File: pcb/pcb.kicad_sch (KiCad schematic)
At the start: 281 parts, among them J1 Conn_01x08_Socket, J2 Conn_01x02_Female, U1 YAAJ_WeAct_BlackPill_Part_Lik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

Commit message: attempting to add RGB
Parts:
- removed BZ1: Buzzer, symbol Device:Buzzer
- removed D18: BAV70, Keebio-Parts:SOT-23_Handsoldering, symbol Diode:BAV70
- removed MX047, MX051.125, MX062, MX063, MX066.100, MX077, MX087, MX089.100, MX099, MX109.100, MX117, MX121, MX132.225, MX136, MX137: MX-NoLED, MX_Only:MXOnly-1U-NoLED, symbol MX_Alps_Hybrid:MX-NoLED
- removed R1, R2: 470, symbol Device:R_Small
- removed R3: R_22K, Keebio-Parts:Resistor, symbol Device:R_Small
- added C1: 100n, schizobovine:C_0603_1608Metric, symbol Device:C_Small
- added FID1: Fiducial, schizobovine:COW, symbol Mechanical:Fiducial
- added LD1, LD10, LD100, LD101, LD102, LD103, LD104, LD105, LD106, LD107, LD108, LD109, LD11, LD110, LD111, LD112, LD113, LD114, LD115, LD116, LD117, LD118, LD119, LD12, LD120, LD121, LD122, LD13, LD14, LD15, LD16, LD17, LD18, LD19, LD2, LD20, LD21, LD22, LD23, LD24, LD25, LD26, LD27, LD28, LD29, LD3, LD30, LD31, LD32, LD33, LD34, LD35, LD36, LD37, LD38, LD39, LD4, LD40, LD41, LD42, LD43, LD44, LD45, LD46, LD47, LD48, LD49, LD5, LD50, LD51, LD52, LD53, LD54, LD55, LD56, LD57, LD58, LD59, LD6, LD60, LD61, LD62, LD63, LD64, LD65, LD66, LD67, LD68, LD69, LD7, LD70, LD71, LD72, LD73, LD74, LD75, LD76, LD77, LD78, LD79, LD8, LD80, LD81, LD82, LD83, LD84, LD85, LD86, LD87, LD88, LD89, LD9, LD90, LD91, LD92, LD93, LD94, LD95, LD96, LD97, LD98, LD99: WS2812B, schizobovine:LED_SK6812MINI_PLCC4_3.1x2.7mm_P1.75mm_reverse_mount, symbol LED:WS2812B
- added N1: Solenoid, schizobovine:solenoid, symbol Mechanical:Housing
- added U2: SN74LVC1G125DBV, Package_TO_SOT_SMD:SOT-23-5, symbol 74xGxx:SN74LVC1G125DBV
- H1, H10, H11, H12, H13, H14, H15, H16, H17, H18, H19, H2, H20, H21, H22, H23, H24, H25, H26, H27, H28, H29, H3, H30, H31, H32, H33, H34, H35, H36, H37, H38, H39, H4, H40, H41, H42, H43, H44, H45, H46, H47, H48, H49, H5, H50, H51, H52, H53, H54, H55, H56, H57, H58, H59, H6, H60, H61, H62, H63, H64, H65, H66, H67, H68, H69, H7, H8, H9: footprint (none) -> MountingHole:MountingHole_3mm
- J1: footprint (none) -> Connector_PinHeader_2.54mm:PinHeader_1x08_P2.54mm_Vertical
- MX000, MX001, MX002, MX003, MX004, MX005, MX006, MX007, MX009, MX012, MX013, MX014, MX015, MX016, MX017, MX018, MX019, MX020, MX021, MX022, MX023, MX024, MX025, MX026, MX027, MX028, MX029, MX030, MX032, MX033, MX034, MX035, MX036, MX037, MX038, MX039, MX040, MX042, MX043, MX044, MX045, MX046, MX048, MX049, MX050, MX052, MX053, MX054, MX055, MX056, MX057, MX058, MX059, MX060, MX065, MX067, MX068, MX069, MX072, MX073, MX074, MX075, MX076, MX078, MX079, MX082, MX083, MX084, MX085, MX086, MX088, MX090, MX091, MX092, MX093, MX094, MX095, MX096, MX097, MX098, MX100, MX101, MX102, MX103, MX104, MX105, MX106, MX107, MX108, MX110, MX111, MX112, MX113, MX114, MX115, MX116, MX117.100, MX120, MX122, MX123, MX124, MX125, MX126, MX130, MX134, MX135: footprint MX_Only:MXOnly-1U-NoLED -> MX_Only:MXOnly-1U-Hotswap
- MX008: footprint (none) -> MX_Only:MXOnly-1U-Hotswap; symbol MX_Alps_Hybrid:MX-LED -> MX_Alps_Hybrid:MX-NoLED
- MX031, MX061, MX064, MX131, MX133: footprint MX_Only:MXOnly-1U-NoLED -> MX_Only:MXOnly-1.5U-Hotswap
- MX041: value MX-LED -> MX-NoLED; footprint (none) -> MX_Only:MXOnly-1.75U-Hotswap; symbol MX_Alps_Hybrid:MX-LED -> MX_Alps_Hybrid:MX-NoLED
- MX041.125: value MX-LED -> MX-NoLED; footprint (none) -> MX_Only:MXOnly-1.25U-Hotswap; symbol MX_Alps_Hybrid:MX-LED -> MX_Alps_Hybrid:MX-NoLED
- MX047.200: footprint MX_Only:MXOnly-1U-NoLED -> MX_Only:MXOnly-ISO-Hotswap
- MX051: footprint MX_Only:MXOnly-1U-NoLED -> MX_Only:MXOnly-2.25U-Hotswap
- MX066: footprint MX_Only:MXOnly-1U-NoLED -> MX_Only:MXOnly-2U-Hotswap
- MX087.200: footprint MX_Only:MXOnly-1U-NoLED -> MX_Only:MXOnly-2U-Hotswap-ReversedStabilizers
- MX089, MX109: footprint MX_Only:MXOnly-1U-NoLED -> MX_Only:MXOnly-2U-Hotswap-ReversedVerticalStabilizers
- MX127: footprint MX_Only:MXOnly-1U-NoLED -> MX_Only:MXOnly-2.75U-Hotswap
- MX127.175: footprint MX_Only:MXOnly-1U-NoLED -> MX_Only:MXOnly-1.75U-Hotswap
- MX132: footprint MX_Only:MXOnly-1U-NoLED -> MX_Only:MXOnly-7U-Hotswap
- R4: footprint Keebio-Parts:Resistor -> Keebio-Parts:Resistor-Hybrid
- U1: footprint Kicad-STM32:YAAJ_WeAct_BlackPill_SWD_2 -> Footprints:YAAJ_WeAct_BlackPill_SWD_2
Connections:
- net +5V: now also C1.1, LD1.1 (VDD), LD10.1 (VDD), LD100.1 (VDD), LD101.1 (VDD), LD102.1 (VDD), LD103.1 (VDD), LD104.1 (VDD), LD105.1 (VDD), LD106.1 (VDD), LD107.1 (VDD), LD108.1 (VDD), LD109.1 (VDD), LD11.1 (VDD), LD110.1 (VDD), LD111.1 (VDD), LD112.1 (VDD), LD113.1 (VDD), LD114.1 (VDD), LD115.1 (VDD), LD116.1 (VDD), LD117.1 (VDD), LD118.1 (VDD), LD119.1 (VDD), LD12.1 (VDD), LD120.1 (VDD), LD121.1 (VDD), LD122.1 (VDD), LD13.1 (VDD), LD14.1 (VDD), LD15.1 (VDD), LD16.1 (VDD), LD17.1 (VDD), LD18.1 (VDD), LD19.1 (VDD), LD2.1 (VDD), LD20.1 (VDD), LD21.1 (VDD), LD22.1 (VDD), LD23.1 (VDD), LD24.1 (VDD), LD25.1 (VDD), LD26.1 (VDD), LD27.1 (VDD), LD28.1 (VDD), LD29.1 (VDD), LD3.1 (VDD), LD30.1 (VDD), LD31.1 (VDD), LD32.1 (VDD), LD33.1 (VDD), LD34.1 (VDD), LD35.1 (VDD), LD36.1 (VDD), LD37.1 (VDD), LD38.1 (VDD), LD39.1 (VDD), LD4.1 (VDD), LD40.1 (VDD), LD41.1 (VDD), LD42.1 (VDD), LD43.1 (VDD), LD44.1 (VDD), LD45.1 (VDD), LD46.1 (VDD), LD47.1 (VDD), LD48.1 (VDD), LD49.1 (VDD), LD5.1 (VDD), LD50.1 (VDD), LD51.1 (VDD), LD52.1 (VDD), LD53.1 (VDD), LD54.1 (VDD), LD55.1 (VDD), LD56.1 (VDD), LD57.1 (VDD), LD58.1 (VDD), LD59.1 (VDD), LD6.1 (VDD), LD60.1 (VDD), LD61.1 (VDD), LD62.1 (VDD), LD63.1 (VDD), LD64.1 (VDD), LD65.1 (VDD), LD66.1 (VDD), LD67.1 (VDD), LD68.1 (VDD), LD69.1 (VDD), LD7.1 (VDD), LD70.1 (VDD), LD71.1 (VDD), LD72.1 (VDD), LD73.1 (VDD), LD74.1 (VDD), LD75.1 (VDD), LD76.1 (VDD), LD77.1 (VDD), LD78.1 (VDD), LD79.1 (VDD), LD8.1 (VDD), LD80.1 (VDD), LD81.1 (VDD), LD82.1 (VDD), LD83.1 (VDD), LD84.1 (VDD), LD85.1 (VDD), LD86.1 (VDD), LD87.1 (VDD), LD88.1 (VDD), LD89.1 (VDD), LD9.1 (VDD), LD90.1 (VDD), LD91.1 (VDD), LD92.1 (VDD), LD93.1 (VDD), LD94.1 (VDD), LD95.1 (VDD), LD96.1 (VDD), LD97.1 (VDD), LD98.1 (VDD), LD99.1 (VDD), U2.5 (VCC)
- net BL_BUZ: no longer U1.7 (PA10)
- net GND: now also C1.2, LD1.3 (VSS), LD10.3 (VSS), LD100.3 (VSS), LD101.3 (VSS), LD102.3 (VSS), LD103.3 (VSS), LD104.3 (VSS), LD105.3 (VSS), LD106.3 (VSS), LD107.3 (VSS), LD108.3 (VSS), LD109.3 (VSS), LD11.3 (VSS), LD110.3 (VSS), LD111.3 (VSS), LD112.3 (VSS), LD113.3 (VSS), LD114.3 (VSS), LD115.3 (VSS), LD116.3 (VSS), LD117.3 (VSS), LD118.3 (VSS), LD119.3 (VSS), LD12.3 (VSS), LD120.3 (VSS), LD121.3 (VSS), LD122.3 (VSS), LD13.3 (VSS), LD14.3 (VSS), LD15.3 (VSS), LD16.3 (VSS), LD17.3 (VSS), LD18.3 (VSS), LD19.3 (VSS), LD2.3 (VSS), LD20.3 (VSS), LD21.3 (VSS), LD22.3 (VSS), LD23.3 (VSS), LD24.3 (VSS), LD25.3 (VSS), LD26.3 (VSS), LD27.3 (VSS), LD28.3 (VSS), LD29.3 (VSS), LD3.3 (VSS), LD30.3 (VSS), LD31.3 (VSS), LD32.3 (VSS), LD33.3 (VSS), LD34.3 (VSS), LD35.3 (VSS), LD36.3 (VSS), LD37.3 (VSS), LD38.3 (VSS), LD39.3 (VSS), LD4.3 (VSS), LD40.3 (VSS), LD41.3 (VSS), LD42.3 (VSS), LD43.3 (VSS), LD44.3 (VSS), LD45.3 (VSS), LD46.3 (VSS), LD47.3 (VSS), LD48.3 (VSS), LD49.3 (VSS), LD5.3 (VSS), LD50.3 (VSS), LD51.3 (VSS), LD52.3 (VSS), LD53.3 (VSS), LD54.3 (VSS), LD55.3 (VSS), LD56.3 (VSS), LD57.3 (VSS), LD58.3 (VSS), LD59.3 (VSS), LD6.3 (VSS), LD60.3 (VSS), LD61.3 (VSS), LD62.3 (VSS), LD63.3 (VSS), LD64.3 (VSS), LD65.3 (VSS), LD66.3 (VSS), LD67.3 (VSS), LD68.3 (VSS), LD69.3 (VSS), LD7.3 (VSS), LD70.3 (VSS), LD71.3 (VSS), LD72.3 (VSS), LD73.3 (VSS), LD74.3 (VSS), LD75.3 (VSS), LD76.3 (VSS), LD77.3 (VSS), LD78.3 (VSS), LD79.3 (VSS), LD8.3 (VSS), LD80.3 (VSS), LD81.3 (VSS), LD82.3 (VSS), LD83.3 (VSS), LD84.3 (VSS), LD85.3 (VSS), LD86.3 (VSS), LD87.3 (VSS), LD88.3 (VSS), LD89.3 (VSS), LD9.3 (VSS), LD90.3 (VSS), LD91.3 (VSS), LD92.3 (VSS), LD93.3 (VSS), LD94.3 (VSS), LD95.3 (VSS), LD96.3 (VSS), LD97.3 (VSS), LD98.3 (VSS), LD99.3 (VSS), U2.1, U2.3 (GND)
- net MOSI_NUM: no longer MX008.3 (LED)
- net SCK_CAPS: no longer MX041.125.3 (LED), MX041.3 (LED)
- net RGB_3v3: now reaches U1.6 (PA9)
- net RGB_3v3: now also U2.2
- new net: LD2.2 (DOUT), LD3.4 (DIN)
- new net: LD1.2 (DOUT), LD2.4 (DIN)
- new net: LD12.2 (DOUT), LD13.4 (DIN)
- new net: LD11.2 (DOUT), LD12.4 (DIN)
- new net: LD50.2 (DOUT), LD51.4 (DIN)
- new net: LD49.2 (DOUT), LD50.4 (DIN)
- new net: LD55.2 (DOUT), LD56.4 (DIN)
- new net: LD54.2 (DOUT), LD55.4 (DIN)
- new net: LD100.4 (DIN), LD99.2 (DOUT)
- new net: LD98.2 (DOUT), LD99.4 (DIN)
- new net: LD104.2 (DOUT), LD105.4 (DIN)
- new net: LD103.2 (DOUT), LD104.4 (DIN)
- new net: LD81.2 (DOUT), LD82.4 (DIN)
- new net: LD80.2 (DOUT), LD81.4 (DIN)
- new net: LD21.2 (DOUT), LD22.4 (DIN)
- new net: LD20.2 (DOUT), LD21.4 (DIN)
- new net: LD29.2 (DOUT), LD30.4 (DIN)
- new net: LD28.2 (DOUT), LD29.4 (DIN)
- new net: LD82.2 (DOUT), LD83.4 (DIN)
- new net: LD39.2 (DOUT), LD40.4 (DIN)
- new net: LD38.2 (DOUT), LD39.4 (DIN)
- new net: LD34.2 (DOUT), LD35.4 (DIN)
- new net: LD33.2 (DOUT), LD34.4 (DIN)
- new net: LD79.2 (DOUT), LD80.4 (DIN)
- new net: LD101.2 (DOUT), LD102.4 (DIN)
- new net: LD100.2 (DOUT), LD101.4 (DIN)
- new net: LD18.2 (DOUT), LD19.4 (DIN)
- new net: LD17.2 (DOUT), LD18.4 (DIN)
- new net: LD14.2 (DOUT), LD15.4 (DIN)
- new net: LD13.2 (DOUT), LD14.4 (DIN)
- new net: LD22.2 (DOUT), LD23.4 (DIN)
- new net: LD27.2 (DOUT), LD28.4 (DIN)
- new net: LD32.2 (DOUT), LD33.4 (DIN)
- new net: LD87.2 (DOUT), LD88.4 (DIN)
- new net: LD86.2 (DOUT), LD87.4 (DIN)
- new net: LD31.2 (DOUT), LD32.4 (DIN)
- new net: LD30.2 (DOUT), LD31.4 (DIN)
- new net: LD42.2 (DOUT), LD43.4 (DIN)
- new net: LD41.2 (DOUT), LD42.4 (DIN)
- new net: LD118.2 (DOUT), LD119.4 (DIN)
- new net: LD117.2 (DOUT), LD118.4 (DIN)
- new net: LD61.2 (DOUT), LD62.4 (DIN)
- new net: LD60.2 (DOUT), LD61.4 (DIN)
- new net: LD16.2 (DOUT), LD17.4 (DIN)
- new net: LD15.2 (DOUT), LD16.4 (DIN)
- new net: LD53.2 (DOUT), LD54.4 (DIN)
- new net: LD37.2 (DOUT), LD38.4 (DIN)
- new net: LD52.2 (DOUT), LD53.4 (DIN)
- new net: LD51.2 (DOUT), LD52.4 (DIN)
- new net: LD71.2 (DOUT), LD72.4 (DIN)
- new net: LD70.2 (DOUT), LD71.4 (DIN)
- new net: LD19.2 (DOUT), LD20.4 (DIN)
- new net: LD89.2 (DOUT), LD90.4 (DIN)
- new net: LD88.2 (DOUT), LD89.4 (DIN)
- new net: LD36.2 (DOUT), LD37.4 (DIN)
- new net: LD35.2 (DOUT), LD36.4 (DIN)
- new net: LD69.2 (DOUT), LD70.4 (DIN)
- new net: LD68.2 (DOUT), LD69.4 (DIN)
- new net: LD77.2 (DOUT), LD78.4 (DIN)
- new net: LD76.2 (DOUT), LD77.4 (DIN)
- new net: LD78.2 (DOUT), LD79.4 (DIN)
- new net: LD108.2 (DOUT), LD109.4 (DIN)
- new net: LD107.2 (DOUT), LD108.4 (DIN)
- new net: LD24.2 (DOUT), LD25.4 (DIN)
- new net: LD23.2 (DOUT), LD24.4 (DIN)
- new net: LD57.2 (DOUT), LD58.4 (DIN)
- new net: LD56.2 (DOUT), LD57.4 (DIN)
- new net: LD7.2 (DOUT), LD8.4 (DIN)
- new net: LD6.2 (DOUT), LD7.4 (DIN)
- new net: LD75.2 (DOUT), LD76.4 (DIN)
- new net: LD72.2 (DOUT), LD73.4 (DIN)
- new net: LD59.2 (DOUT), LD60.4 (DIN)
- new net: LD10.4 (DIN), LD9.2 (DOUT)
- new net: LD8.2 (DOUT), LD9.4 (DIN)
- new net: LD74.2 (DOUT), LD75.4 (DIN)
- new net: LD73.2 (DOUT), LD74.4 (DIN)
- new net: LD97.2 (DOUT), LD98.4 (DIN)
- new net: LD112.2 (DOUT), LD113.4 (DIN)
- new net: LD111.2 (DOUT), LD112.4 (DIN)
- new net: LD67.2 (DOUT), LD68.4 (DIN)
- new net: LD84.2 (DOUT), LD85.4 (DIN)
- new net: LD83.2 (DOUT), LD84.4 (DIN)
- new net: LD48.2 (DOUT), LD49.4 (DIN)
- new net: LD45.2 (DOUT), LD46.4 (DIN)
- new net: LD44.2 (DOUT), LD45.4 (DIN)
- new net: LD46.2 (DOUT), LD47.4 (DIN)
- new net: LD26.2 (DOUT), LD27.4 (DIN)
- new net: LD25.2 (DOUT), LD26.4 (DIN)
- new net: LD120.2 (DOUT), LD121.4 (DIN)
- new net: LD119.2 (DOUT), LD120.4 (DIN)
- new net: LD43.2 (DOUT), LD44.4 (DIN)
- new net: LD47.2 (DOUT), LD48.4 (DIN)
- new net: LD3.2 (DOUT), LD4.4 (DIN)
- new net: LD106.2 (DOUT), LD107.4 (DIN)
- new net: LD40.2 (DOUT), LD41.4 (DIN)
- new net: LD110.2 (DOUT), LD111.4 (DIN)
- new net: LD109.2 (DOUT), LD110.4 (DIN)
- new net: LD96.2 (DOUT), LD97.4 (DIN)
- new net: LD102.2 (DOUT), LD103.4 (DIN)
- new net: LD10.2 (DOUT), LD11.4 (DIN)
- new net: LD65.2 (DOUT), LD66.4 (DIN)
- new net: LD64.2 (DOUT), LD65.4 (DIN)
- new net: LD85.2 (DOUT), LD86.4 (DIN)
- new net: LD95.2 (DOUT), LD96.4 (DIN)
- new net: LD5.2 (DOUT), LD6.4 (DIN)
- new net: LD4.2 (DOUT), LD5.4 (DIN)
- new net: LD66.2 (DOUT), LD67.4 (DIN)
- new net: LD94.2 (DOUT), LD95.4 (DIN)
- new net: LD116.2 (DOUT), LD117.4 (DIN)
- new net: LD115.2 (DOUT), LD116.4 (DIN)
- new net: LD105.2 (DOUT), LD106.4 (DIN)
- new net: LD121.2 (DOUT), LD122.4 (DIN)
- new net: LD113.2 (DOUT), LD114.4 (DIN)
- new net: LD63.2 (DOUT), LD64.4 (DIN)
- new net: LD92.2 (DOUT), LD93.4 (DIN)
- new net: LD91.2 (DOUT), LD92.4 (DIN)
- new net: LD114.2 (DOUT), LD115.4 (DIN)
- new net: LD62.2 (DOUT), LD63.4 (DIN)
- new net: LD58.2 (DOUT), LD59.4 (DIN)
- new net: LD90.2 (DOUT), LD91.4 (DIN)
- new net: LD93.2 (DOUT), LD94.4 (DIN)
- new net RGB_5V: LD1.4 (DIN), U2.4

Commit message: RGB added
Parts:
- removed D53: BAV70, Keebio-Parts:SOT-23_Handsoldering, symbol Diode:BAV70
- removed H54, H56: MountingHole, MountingHole:MountingHole_3mm, symbol Mechanical:MountingHole
- removed MX127: MX-NoLED, MX_Only:MXOnly-2.75U-Hotswap, symbol MX_Alps_Hybrid:MX-NoLED
- added D18: BAV70, Keebio-Parts:SOT-23_Handsoldering, symbol Diode:BAV70
- added FID2: Fiducial, schizobovine:oshw, symbol Mechanical:Fiducial
- added FID3, FID4: Fiducial, schizobovine:qmk_logo, symbol Mechanical:Fiducial
- added FID5: Fiducial, schizobovine:COW, symbol Mechanical:Fiducial
- added H100, H101, H108, H110, H111, H112, H113, H114, H115, H116, H117, H118, H119, H120, H121, H122, H123, H124, H125, H70, H71, H74, H75, H76, H77, H78, H79, H81, H82, H83, H84, H85, H86, H87, H88, H89, H90, H91, H95, H96, H97, H98: MountingHole, schizobovine:MountingHole_3.1mm_M2.5_solderable, symbol Mechanical:MountingHole
- added LD123, LD124, LD125: WS2812B, schizobovine:LED_SK6812MINI_PLCC4_3.1x2.7mm_P1.75mm_reverse_mount, symbol schizobovine:SK6812MINI
- added MX077, MX10, MX11: MX-NoLED, MX_Only:MXOnly-1U-Hotswap, symbol MX_Alps_Hybrid:MX-NoLED
- H10, H17, H18, H19, H2, H20, H21, H22, H24, H25, H26, H27, H28, H29, H3, H32, H34, H36, H37, H38, H4, H42, H44, H45, H46, H47, H48, H5, H50, H53, H55, H57, H8, H9: footprint MountingHole:MountingHole_3mm -> schizobovine:MountingHole_3.1mm_M2.5_solderable
- LD1, LD10, LD100, LD101, LD102, LD103, LD104, LD105, LD106, LD107, LD108, LD109, LD11, LD110, LD111, LD112, LD113, LD114, LD115, LD116, LD117, LD118, LD119, LD12, LD120, LD121, LD122, LD13, LD14, LD15, LD16, LD17, LD18, LD19, LD2, LD20, LD21, LD22, LD23, LD24, LD25, LD26, LD27, LD28, LD29, LD3, LD30, LD31, LD32, LD33, LD34, LD35, LD36, LD37, LD38, LD39, LD4, LD40, LD41, LD42, LD43, LD44, LD45, LD46, LD47, LD48, LD49, LD5, LD50, LD51, LD52, LD53, LD54, LD55, LD56, LD57, LD58, LD59, LD6, LD60, LD61, LD62, LD63, LD64, LD65, LD66, LD67, LD68, LD69, LD7, LD70, LD71, LD72, LD73, LD74, LD75, LD76, LD77, LD78, LD79, LD8, LD80, LD81, LD82, LD83, LD84, LD85, LD86, LD87, LD88, LD89, LD9, LD90, LD91, LD92, LD93, LD94, LD95, LD96, LD97, LD98, LD99: symbol LED:WS2812B -> schizobovine:SK6812MINI
- MX047: renamed from MX047.200; footprint MX_Only:MXOnly-ISO-Hotswap -> MX_Only:MXOnly-2.25U-Hotswap-ReversedStabilizers
- MX087: renamed from MX087.200; footprint MX_Only:MXOnly-2U-Hotswap-ReversedStabilizers -> MX_Only:MXOnly-1U-Hotswap
- MX117: renamed from MX117.100; footprint MX_Only:MXOnly-1U-Hotswap -> MX_Only:MXOnly-1.5U-Hotswap
- MX131, MX133: footprint MX_Only:MXOnly-1.5U-Hotswap -> MX_Only:MXOnly-1U-Hotswap
- MX132: footprint MX_Only:MXOnly-7U-Hotswap -> MX_Only:MXOnly-6U-Centered-Hotswap
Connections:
- net +5V: now also LD123.1 (VDD), LD124.1 (VDD), LD125.1 (VDD)
- net COL2: now also MX10.1 (COL)
- net COL3: now also MX11.1 (COL)
- net COL7: now also MX077.1 (COL); no longer MX127.175.2 (ROW)
- net GND: now also LD123.3 (VSS), LD124.3 (VSS), LD125.3 (VSS)
- net ROW6: now also D18.3 (K)
- net at LD33.4 (DIN): now also LD123.2 (DOUT); no longer LD32.2 (DOUT)
- net at LD118.4 (DIN): now also LD125.2 (DOUT); no longer LD117.2 (DOUT)
- net at D47.2 (A): now also MX077.2 (ROW)
- net at D52.2 (A): now also MX127.175.2 (ROW)
- net at LD120.4 (DIN): now also LD124.2 (DOUT); no longer LD119.2 (DOUT)
- new net: D18.1 (A), MX10.2 (ROW)
- new net: D18.2 (A), MX11.2 (ROW)
- new net: LD117.2 (DOUT), LD125.4 (DIN)
- new net: LD123.4 (DIN), LD32.2 (DOUT)
- new net: LD119.2 (DOUT), LD124.4 (DIN)
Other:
- moved on the sheet: H1, H10, H11, H12, H13, H14, H15, H16, H17, H18, H19, H2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

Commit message: finished RGB
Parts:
- added J3: Aux 5V, TerminalBlock:TerminalBlock_bornier-2_P5.08mm, symbol Connector:Conn_01x02_Female
- added J4: Aux 5V, Connector_Wire:SolderWire-2sqmm_1x02_P7.8mm_D2mm_OD3.9mm, symbol Connector:Conn_01x02_Female
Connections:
- net +5V: now also J3.2 (Pin_2), J4.2 (Pin_2)
- net GND: now also J3.1 (Pin_1), J4.1 (Pin_1)
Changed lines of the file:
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@@
   (junction (at 165.1 90.17) (diameter 0) (color 0 0 0 0)
   )
+  (junction (at 96.774 204.978) (diameter 0) (color 0 0 0 0)
+  )
   (junction (at 419.1 133.35) (diameter 0) (color 0 0 0 0)
   )
@@
   (junction (at 372.11 35.56) (diameter 0) (color 0 0 0 0)
   )
+  (junction (at 96.774 202.438) (diameter 0) (color 0 0 0 0)
+  )
   (junction (at 589.28 133.35) (diameter 0) (color 0 0 0 0)
   )
@@
     (stroke (width 0) (type default))
   )
+  (wire (pts (xy 104.902 202.438) (xy 96.774 202.438))
+    (stroke (width 0) (type default))
+  )
   (wire (pts (xy 589.28 68.58) (xy 589.28 90.17))
     (stroke (width 0) (type default))
@@
     (stroke (width 0) (type default))
   )
+  (wire (pts (xy 104.902 204.978) (xy 96.774 204.978))
+    (stroke (width 0) (type default))
+  )
   (wire (pts (xy 612.14 52.07) (xy 612.14 57.15))
     (stroke (width 0) (type default))
@@
     (stroke (width 0) (type default))
   )
+  (wire (pts (xy 88.392 202.438) (xy 96.774 202.438))
+    (stroke (width 0) (type default))
+  )
   (wire (pts (xy 259.08 35.56) (xy 250.19 35.56))
     (stroke (width 0) (type default))
@@
     (stroke (width 0) (type default))
   )
+  (wire (pts (xy 88.392 204.978) (xy 96.774 204.978))
+    (stroke (width 0) (type default))
+  )
   (wire (pts (xy 532.13 46.99) (xy 532.13 68.58))
     (stroke (width 0) (type default))
@@
     )
   )
+  (symbol (lib_id "power:GND") (at 96.774 204.978 0) (unit 1)
+    (in_bom yes) (on_board yes) (dnp no) (fields_autoplaced)
+    (property "Reference" "#PWR0238" (at 96.774 211.328 0)
+      (effects (font (size 1.27 1.27)) hide)
+    )
+    (property "Value" "GND" (at 96.774 209.5405 0)
+      (effects (font (size 1.27 1.27)))
+    )
+    (property "Footprint" "" (at 96.774 204.978 0)
+      (effects (font (size 1.27 1.27)) hide)
+    )
+    (property "Datasheet" "" (at 96.774 204.978 0)
+      (effects (font (size 1.27 1.27)) hide)
+    )
+    (pin "1")
+    (instances
+      (project "pcb"
+        (path "/e63e39d7-6ac0-4ffd-8aa3-1841a4541b55"
+          (reference "#PWR0238") (unit 1)
+        )
+      )
+    )
+  )
   (symbol (lib_id "MX_Alps_Hybrid:MX-NoLED") (at 500.38 91.44 0) (unit 1)
     (in_bom yes) (on_board yes) (dnp no)
@@
     )
   )
+  (symbol (lib_id "Connector:Conn_01x02_Female") (at 109.982 204.978 0) (mirror x) (unit 1)
+    (in_bom yes) (on_board yes) (dnp no)
+    (property "Reference" "J3" (at 110.998 204.978 0)
+      (effects (font (size 1.27 1.27)) (justify left))
+    )
+    (property "Value" "Aux 5V" (at 110.998 202.438 0)
+      (effects (font (size 1.27 1.27)) (justify left))
+    )
+    (property "Footprint" "TerminalBlock:TerminalBlock_bornier-2_P5.08mm" (at 109.982 204.978 0)
+      (effects (font (size 1.27 1.27)) hide)
+    )
+    (property "Datasheet" "~" (at 109.982 204.978 0)
+      (effects (font (size 1.27 1.27)) hide)
+    )
+    (pin "1")
+    (pin "2")
+    (instances
+      (project "pcb"
+        (path "/e63e39d7-6ac0-4ffd-8aa3-1841a4541b55"
+          (reference "J3") (unit 1)
+        )
+      )
+    )
+  )
   (symbol (lib_id "MX_Alps_Hybrid:MX-NoLED") (at 585.47 134.62 0) (unit 1)
     (in_bom yes) (on_board yes) (dnp no)
@@
     )
   )
+  (symbol (lib_id "Connector:Conn_01x02_Female") (at 83.312 204.978 180) (unit 1)
+    (in_bom yes) (on_board yes) (dnp no)
+    (property "Reference" "J4" (at 82.296 204.978 0)
+      (effects (font (size 1.27 1.27)) (justify left))
+    )
+    (property "Value" "Aux 5V" (at 82.296 202.438 0)
+      (effects (font (size 1.27 1.27)) (justify left))
+    )
+    (property "Footprint" "Connector_Wire:SolderWire-2sqmm_1x02_P7.8mm_D2mm_OD3.9mm" (at 83.312 204.978 0)
+      (effects (font (size 1.27 1.27)) hide)
+    )
+    (property "Datasheet" "~" (at 83.312 204.978 0)
+      (effects (font (size 1.27 1.27)) hide)
+    )
+    (pin "1")
+    (pin "2")
+    (instances
+      (project "pcb"
+        (path "/e63e39d7-6ac0-4ffd-8aa3-1841a4541b55"
+          (reference "J4") (unit 1)
+        )
+      )
+    )
+  )
   (symbol (lib_id "schizobovine:SK6812MINI") (at 550.164 365.76 0) (unit 1)
     (in_bom yes) (on_board yes) (dnp no)
@@
         )
       )
+    )
+  )
+  (symbol (lib_id "power:+5V") (at 96.774 202.438 0) (unit 1)
+    (in_bom yes) (on_board yes) (dnp no) (fields_autoplaced)
+    (property "Reference" "#PWR0260" (at 96.774 206.248 0)
+      (effects (font (size 1.27 1.27)) hide)
+    )
+    (property "Value" "+5V" (at 96.774 198.8335 0)
+      (effects (font (size 1.27 1.27)))
+    )
+    (property "Footprint" "" (at 96.774 202.438 0)
+      (effects (font (size 1.27 1.27)) hide)
+    )
+    (property "Datasheet" "" (at 96.774 202.438 0)
+      (effects (font (size 1.27 1.27)) hide)
+    )
+    (pin "1")
+    (instances
+      (project "pcb"
+        (path "/e63e39d7-6ac0-4ffd-8aa3-1841a4541b55"
+          (reference "#PWR0260") (unit 1)
+        )
+      )

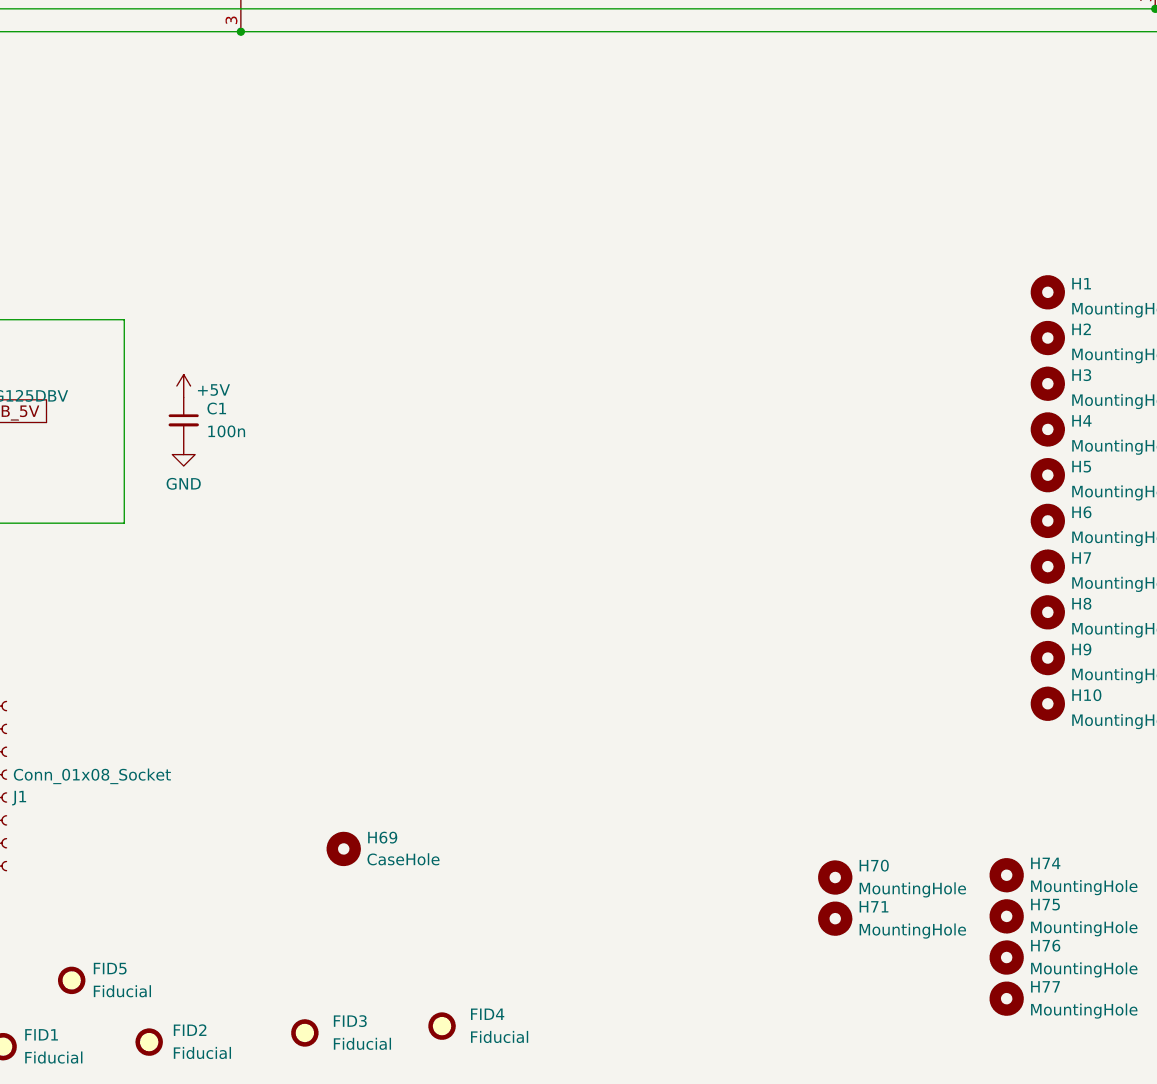
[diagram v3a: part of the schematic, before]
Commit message: rev 4 with moved holes and caps
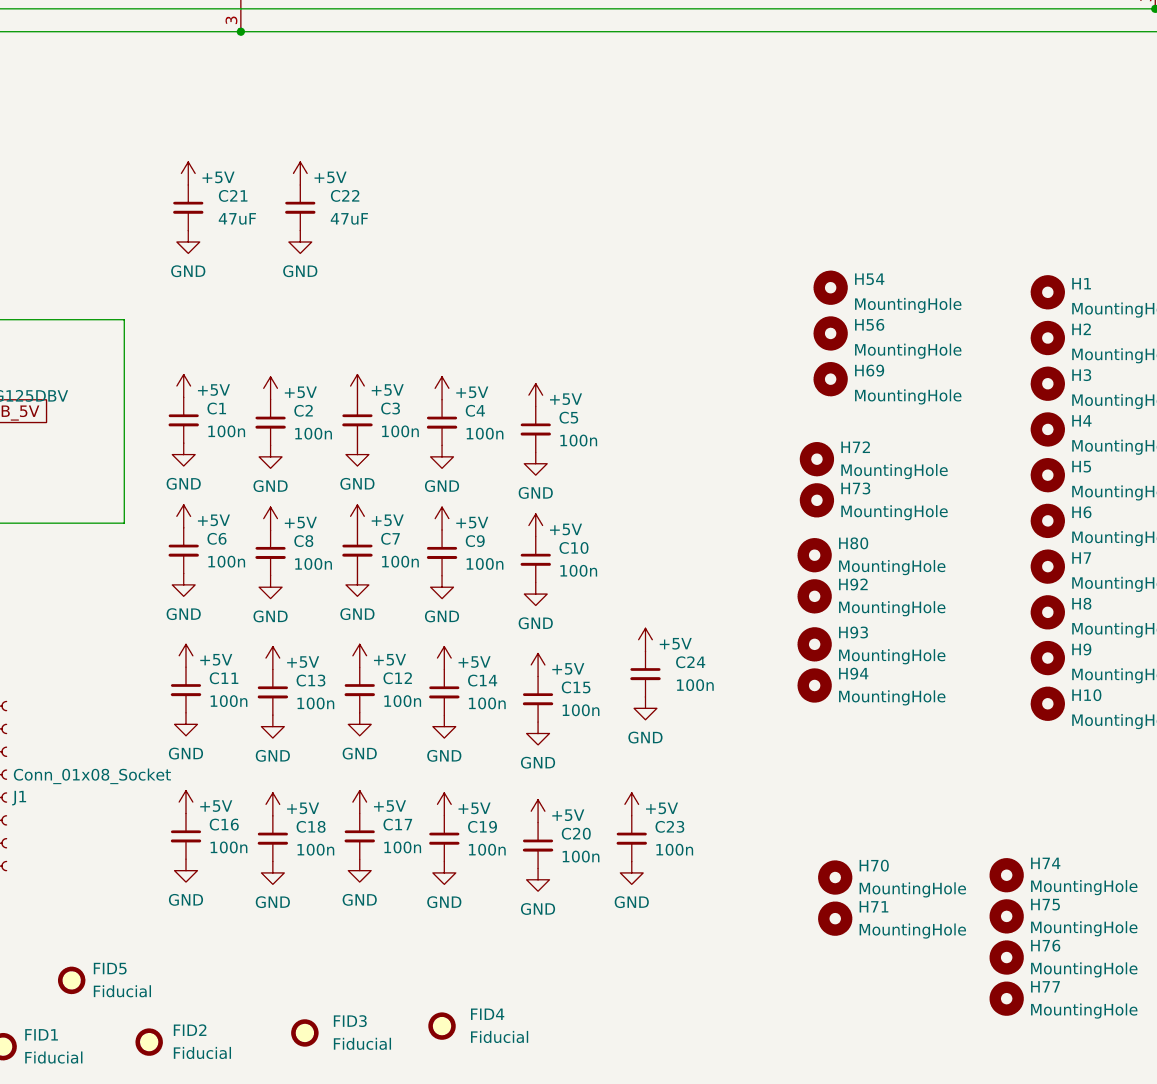
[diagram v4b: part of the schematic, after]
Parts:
- added C10, C11, C12, C13, C14, C15, C16, C17, C18, C19, C2, C20, C23, C3, C4, C5, C6, C7, C8, C9: 100n, schizobovine:C_0603_1608Metric, symbol Device:C_Small
- added C21, C22: 47uF, Capacitor_THT:CP_Radial_D10.0mm_P2.50mm_P5.00mm, symbol Device:C_Small
- added C24: 100n, schizobovine:C_0805_2012Metric, symbol Device:C_Small
- added H54, H56, H72, H73, H80: MountingHole, schizobovine:MountingHole_2.6mm_M2_4mm_dia_solderable_tighter_hole, symbol Mechanical:MountingHole
- added H92, H93, H94: MountingHole, schizobovine:MountingHole_3.0mm_M2_5mm_dia_solderable, symbol Mechanical:MountingHole
- H1, H11, H12, H13, H14, H15, H16, H43, H51, H6, H60, H61, H62, H63, H64, H65, H66, H67, H68, H7: footprint MountingHole:MountingHole_3mm -> schizobovine:MountingHole_3.0mm_M2_5mm_dia_solderable
- H10, H100, H101, H108, H110, H111, H112, H113, H114, H115, H116, H117, H118, H119, H124, H17, H18, H19, H2, H20, H21, H22, H24, H25, H26, H27, H28, H29, H3, H32, H34, H36, H37, H38, H4, H42, H44, H45, H46, H47, H48, H5, H50, H53, H55, H57, H74, H75, H76, H77, H78, H79, H8, H81, H82, H83, H84, H87, H89, H9, H90, H91, H95, H96, H97, H98: footprint schizobovine:MountingHole_3.1mm_M2.5_solderable -> schizobovine:MountingHole_2.6mm_M2_4mm_dia_solderable_tighter_hole
- H120, H121, H122, H123, H125, H70, H71, H85, H86, H88: footprint schizobovine:MountingHole_3.1mm_M2.5_solderable -> schizobovine:MountingHole_3.0mm_M2_5mm_dia_solderable
- H23, H30, H31, H33, H35, H39, H40, H41, H49, H52, H58, H59: footprint MountingHole:MountingHole_3mm -> schizobovine:MountingHole_2.6mm_M2_4mm_dia_solderable_tighter_hole
- H69: value CaseHole -> MountingHole; footprint MountingHole:MountingHole_3mm -> schizobovine:MountingHole_2.6mm_M2_4mm_dia_solderable_tighter_hole
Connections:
- net +5V: now also C10.1, C11.1, C12.1, C13.1, C14.1, C15.1, C16.1, C17.1, C18.1, C19.1, C2.1, C20.1, C21.1, C22.1, C23.1, C24.1, C3.1, C4.1, C5.1, C6.1, C7.1, C8.1, C9.1
- net GND: now also C10.2, C11.2, C12.2, C13.2, C14.2, C15.2, C16.2, C17.2, C18.2, C19.2, C2.2, C20.2, C21.2, C22.2, C23.2, C24.2, C3.2, C4.2, C5.2, C6.2, C7.2, C8.2, C9.2
